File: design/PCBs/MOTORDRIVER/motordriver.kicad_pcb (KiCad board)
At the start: 2 copper layers, 1 part, among them U1 TMC4671-LA

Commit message: update docs
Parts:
- moved U1 26.6 mm to (145.0, 104.0)
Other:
- board outline added: 47.5 x 25 mm
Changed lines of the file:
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@@
 		(pad_to_mask_clearance 0)
 		(allow_soldermask_bridges_in_footprints no)
-		(grid_origin 165.027501 121.5)
+		(grid_origin 145.027501 104)
 		(pcbplotparams
 			(layerselection 0x00010fc_ffffffff)
@@
 	(footprint "Custom_Motor_Driver:QFN76_10P5X6P5_TRI"
 		(layer "F.Cu")
-		(at 165.027501 121.5)
+		(at 145.027501 104)
 		(tags "TMC4671-LA ")
 		(property "Reference" "U1"
@@
 		)
 	)
-	(gr_arc
-		(start 190.027501 135)
-		(mid 188.855928 137.828427)
-		(end 186.027501 139)
+	(gr_line
+		(start 167.627501 92.821401)
+		(end 167.627501 113.821401)
 		(stroke
-			(width 0.2)
+			(width 0.05)
 			(type default)
 		)
-		(layer "F.Cu")
+		(layer "Edge.Cuts")
 	)
-	(gr_arc
-		(start 144.027501 139)
-		(mid 141.199074 137.828427)
-		(end 140.027501 135)
+	(gr_line
+		(start 165.627501 115.821401)
+		(end 122.127501 115.821401)
 		(stroke
-			(width 0.2)
+			(width 0.05)
 			(type default)
 		)
-		(layer "F.Cu")
+		(layer "Edge.Cuts")
 	)
 	(gr_line
-		(start 140.027501 135)
-		(end 140.027501 105.5)
+		(start 120.127501 113.821401)
+		(end 120.127501 92.821401)
 		(stroke
-			(width 0.2)
+			(width 0.05)
 			(type default)
 		)
-		(layer "F.Cu")
+		(layer "Edge.Cuts")
 	)
 	(gr_arc
-		(start 186.027501 101.5)
-		(mid 188.855927 102.671573)
-		(end 190.027501 105.5)
+		(start 165.627501 90.821401)
+		(mid 167.041714 91.407188)
+		(end 167.627501 92.821401)
 		(stroke
-			(width 0.2)
+			(width 0.05)
 			(type default)
 		)
-		(layer "F.Cu")
+		(layer "Edge.Cuts")
 	)
-	(gr_line
-		(start 190.027501 105.5)
-		(end 190.027501 135)
+	(gr_arc
+		(start 120.127501 92.821401)
+		(mid 120.713287 91.407188)
+		(end 122.127501 90.821401)
 		(stroke
-			(width 0.2)
+			(width 0.05)
 			(type default)
 		)
-		(layer "F.Cu")
+		(layer "Edge.Cuts")
 	)
-	(gr_line
-		(start 186.027501 139)
-		(end 144.027501 139)
+	(gr_arc
+		(start 167.627501 113.821401)
+		(mid 167.041715 115.235615)
+		(end 165.627501 115.821401)
 		(stroke
-			(width 0.2)
+			(width 0.05)
 			(type default)
 		)
-		(layer "F.Cu")
+		(layer "Edge.Cuts")
 	)
 	(gr_line
-		(start 144.027501 101.5)
-		(end 186.027501 101.5)
+		(start 122.127501 90.821401)
+		(end 165.627501 90.821401)
 		(stroke
-			(width 0.2)
+			(width 0.05)
 			(type default)
 		)
-		(layer "F.Cu")
+		(layer "Edge.Cuts")
 	)
 	(gr_arc
-		(start 140.027501 105.5)
-		(mid 141.199074 102.671573)
-		(end 144.027501 101.5)
+		(start 122.127501 115.821401)
+		(mid 120.713287 115.235615)
+		(end 120.127501 113.821401)
 		(stroke
-			(width 0.2)
+			(width 0.05)
 			(type default)
 		)
-		(layer "F.Cu")
+		(layer "Edge.Cuts")
 	)
 )

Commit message: update motordriver
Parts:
- added U2: HIP2100_DFN, Package_DFN_QFN:DFN-12-1EP_4x4mm_P0.5mm_EP2.66x3.38mm, F.Cu at (130.6, 102.8)

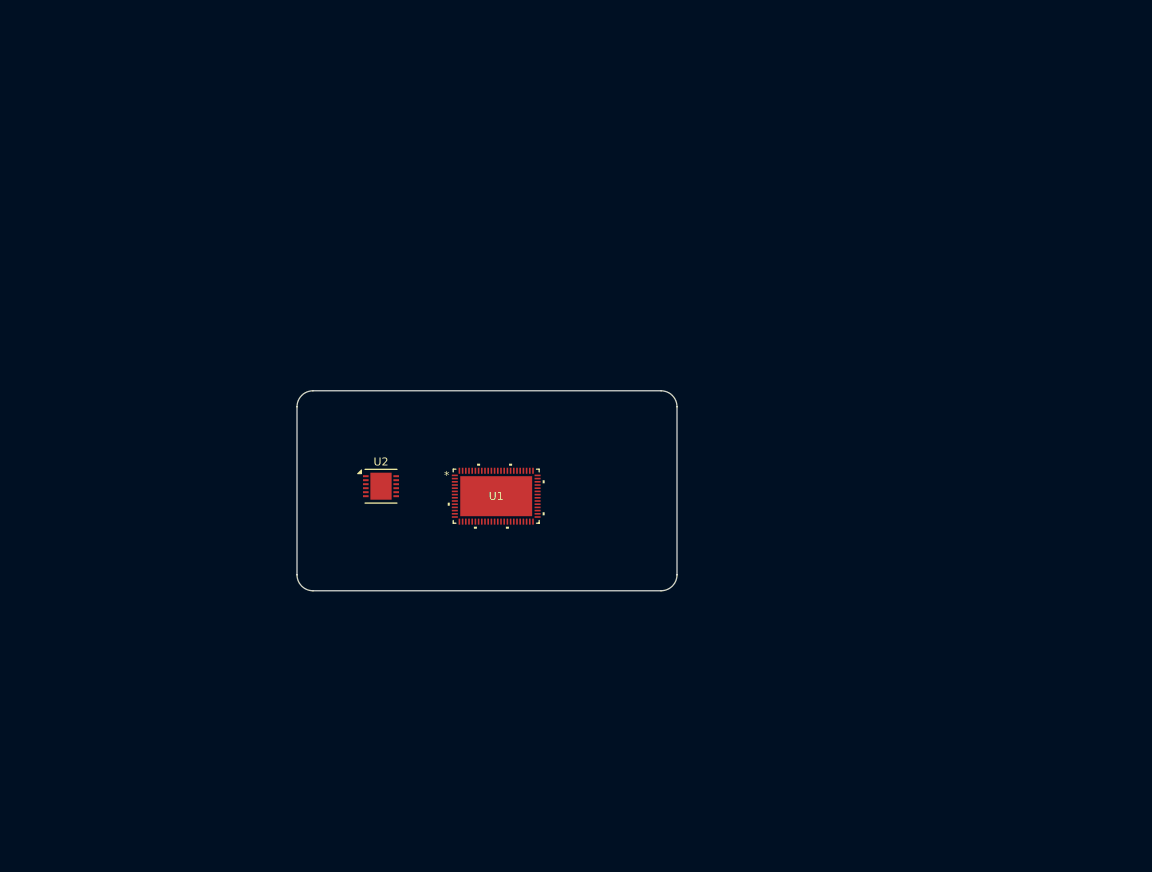
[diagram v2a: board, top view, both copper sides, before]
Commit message: cleaned up, added values and footprints
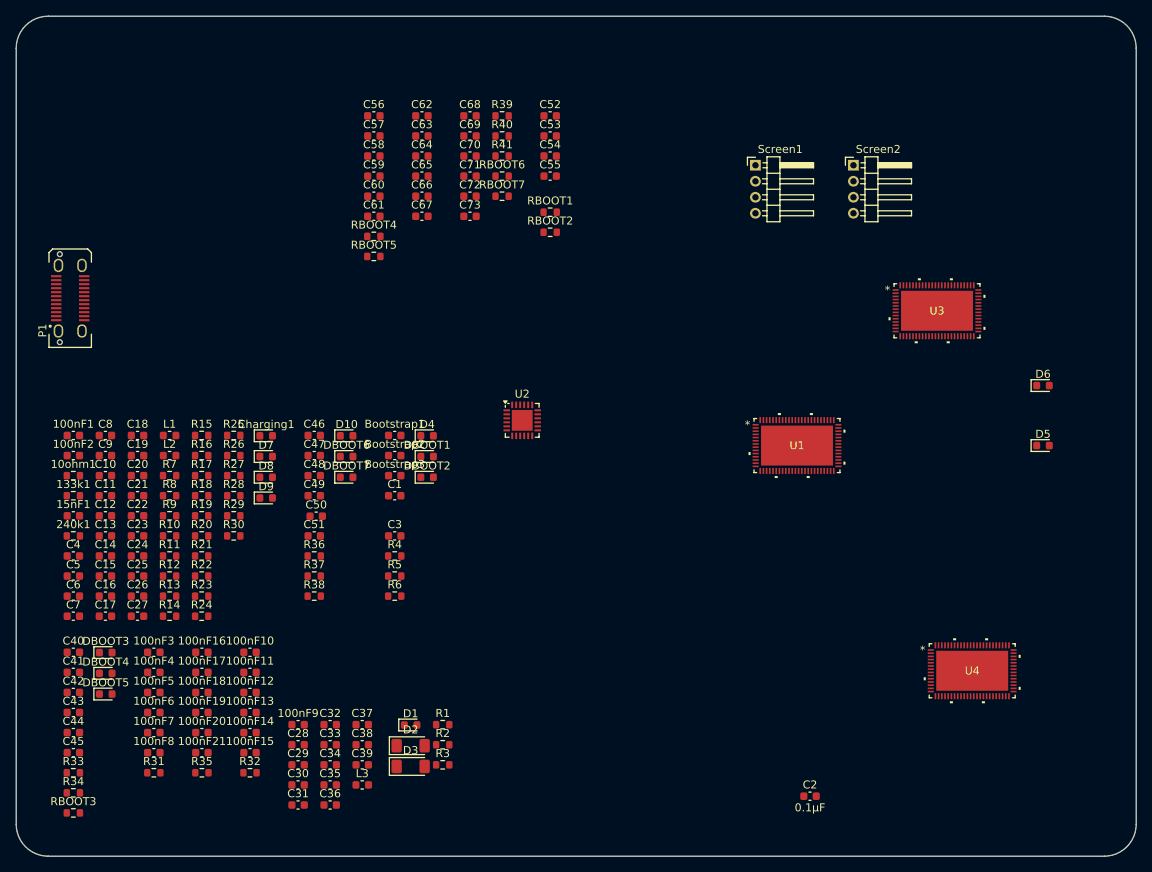
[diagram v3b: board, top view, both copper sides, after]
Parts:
- added 100nF1: C, Capacitor_SMD:C_0603_1608Metric, F.Cu at (92.2, 96.4)
- added 100nF10: C, Capacitor_SMD:C_0603_1608Metric, F.Cu at (114.3, 123.5)
- added 100nF11: C, Capacitor_SMD:C_0603_1608Metric, F.Cu at (114.3, 126.0)
- added 100nF12: C, Capacitor_SMD:C_0603_1608Metric, F.Cu at (114.3, 128.5)
- added 100nF13: C, Capacitor_SMD:C_0603_1608Metric, F.Cu at (114.3, 131.0)
- added 100nF14: C, Capacitor_SMD:C_0603_1608Metric, F.Cu at (114.3, 133.6)
- added 100nF15: C, Capacitor_SMD:C_0603_1608Metric, F.Cu at (114.3, 136.1)
- added 100nF16: C, Capacitor_SMD:C_0603_1608Metric, F.Cu at (108.2, 123.5)
- added 100nF17: C, Capacitor_SMD:C_0603_1608Metric, F.Cu at (108.2, 126.0)
- added 100nF18: C, Capacitor_SMD:C_0603_1608Metric, F.Cu at (108.2, 128.5)
- added 100nF19: C, Capacitor_SMD:C_0603_1608Metric, F.Cu at (108.2, 131.0)
- added 100nF2: C, Capacitor_SMD:C_0603_1608Metric, F.Cu at (92.2, 98.9)
- added 100nF20: C, Capacitor_SMD:C_0603_1608Metric, F.Cu at (108.2, 133.6)
- added 100nF21: C, Capacitor_SMD:C_0603_1608Metric, F.Cu at (108.2, 136.1)
- added 100nF3: C, Capacitor_SMD:C_0603_1608Metric, F.Cu at (102.2, 123.5)
- added 100nF4: C, Capacitor_SMD:C_0603_1608Metric, F.Cu at (102.2, 126.0)
- added 100nF5: C, Capacitor_SMD:C_0603_1608Metric, F.Cu at (102.2, 128.5)
- added 100nF6: C, Capacitor_SMD:C_0603_1608Metric, F.Cu at (102.2, 131.0)
- added 100nF7: C, Capacitor_SMD:C_0603_1608Metric, F.Cu at (102.2, 133.6)
- added 100nF8: C, Capacitor_SMD:C_0603_1608Metric, F.Cu at (102.2, 136.1)
- added 100nF9: C, Capacitor_SMD:C_0603_1608Metric, F.Cu at (120.3, 132.6)
- added 10ohm1: R, Resistor_SMD:R_0603_1608Metric, F.Cu at (92.2, 101.4)
- added 133k1: R, Resistor_SMD:R_0603_1608Metric, F.Cu at (92.2, 103.9)
- added 15nF1: C, Capacitor_SMD:C_0603_1608Metric, F.Cu at (92.2, 106.5)
- added 240k1: R, Resistor_SMD:R_0603_1608Metric, F.Cu at (92.2, 109.0)
- added Bootstrap1: 0.1µF, Capacitor_SMD:C_0603_1608Metric, F.Cu at (132.3, 96.4)
- added Bootstrap2: 0.1µF, Capacitor_SMD:C_0603_1608Metric, F.Cu at (132.3, 98.9)
- added Bootstrap3: 0.1µF, Capacitor_SMD:C_0603_1608Metric, F.Cu at (132.3, 101.4)
- added C1: 0.1µF, Capacitor_SMD:C_0603_1608Metric, F.Cu at (132.3, 103.9)
- added C10: 0.1µF, Capacitor_SMD:C_0603_1608Metric, F.Cu at (96.2, 101.4)
- added C11: 1µF, Capacitor_SMD:C_0603_1608Metric, F.Cu at (96.2, 103.9)
- added C12: 1µF, Capacitor_SMD:C_0603_1608Metric, F.Cu at (96.2, 106.5)
- added C13: 0.047µF, Capacitor_SMD:C_0603_1608Metric, F.Cu at (96.2, 109.0)
- added C14: 100nF, Capacitor_SMD:C_0603_1608Metric, F.Cu at (96.2, 111.5)
- added C15: 1µF, Capacitor_SMD:C_0603_1608Metric, F.Cu at (96.2, 114.0)
- added C16: 100nF, Capacitor_SMD:C_0603_1608Metric, F.Cu at (96.2, 116.5)
- added C17: 0.1µF, Capacitor_SMD:C_0603_1608Metric, F.Cu at (96.2, 119.0)
- added C18: 0.1µF, Capacitor_SMD:C_0603_1608Metric, F.Cu at (100.2, 96.4)
- added C19: 100nF, Capacitor_SMD:C_0603_1608Metric, F.Cu at (100.2, 98.9)
- added C2: 0.1µF, Capacitor_SMD:C_0603_1608Metric, F.Cu at (184.3, 141.5)
- added C20: 10µF, Capacitor_SMD:C_0603_1608Metric, F.Cu at (100.2, 101.4)
- added C21: 10µF, Capacitor_SMD:C_0603_1608Metric, F.Cu at (100.2, 103.9)
- added C22: 10nF, Capacitor_SMD:C_0603_1608Metric, F.Cu at (100.2, 106.5)
- added C23: 10µF, Capacitor_SMD:C_0603_1608Metric, F.Cu at (100.2, 109.0)
- added C24: 33nF, Capacitor_SMD:C_0603_1608Metric, F.Cu at (100.2, 111.5)
- added C25: 470pF, Capacitor_SMD:C_0603_1608Metric, F.Cu at (100.2, 114.0)
- added C26: 15nF, Capacitor_SMD:C_0603_1608Metric, F.Cu at (100.2, 116.5)
- added C27: 220pF, Capacitor_SMD:C_0603_1608Metric, F.Cu at (100.2, 119.0)
- added C28: 270µF, Capacitor_SMD:C_0603_1608Metric, F.Cu at (120.3, 135.1)
- added C29: 100nF, Capacitor_SMD:C_0603_1608Metric, F.Cu at (120.3, 137.6)
- added C3: 0.1µF, Capacitor_SMD:C_0603_1608Metric, F.Cu at (132.3, 109.0)
- added C30: 100nF, Capacitor_SMD:C_0603_1608Metric, F.Cu at (120.3, 140.1)
- added C31: 100nF, Capacitor_SMD:C_0603_1608Metric, F.Cu at (120.3, 142.6)
- added C32: 100nF, Capacitor_SMD:C_0603_1608Metric, F.Cu at (124.3, 132.6)
- added C33: 100nF, Capacitor_SMD:C_0603_1608Metric, F.Cu at (124.3, 135.1)
- added C34: 100nF, Capacitor_SMD:C_0603_1608Metric, F.Cu at (124.3, 137.6)
- added C35: 100nF, Capacitor_SMD:C_0603_1608Metric, F.Cu at (124.3, 140.1)
- added C36: 100nF, Capacitor_SMD:C_0603_1608Metric, F.Cu at (124.3, 142.6)
- added C37: 100nF, Capacitor_SMD:C_0603_1608Metric, F.Cu at (128.3, 132.6)
- added C38: 10µF, Capacitor_SMD:C_0603_1608Metric, F.Cu at (128.3, 135.1)
- added C39: 100nF, Capacitor_SMD:C_0603_1608Metric, F.Cu at (128.3, 137.6)
- added C4: 2.2µF, Capacitor_SMD:C_0603_1608Metric, F.Cu at (92.2, 111.5)
- added C40: 10µF, Capacitor_SMD:C_0603_1608Metric, F.Cu at (92.2, 123.5)
- added C41: 100nF, Capacitor_SMD:C_0603_1608Metric, F.Cu at (92.2, 126.0)
- added C42: 10µF, Capacitor_SMD:C_0603_1608Metric, F.Cu at (92.2, 128.5)
- added C43: 100nF, Capacitor_SMD:C_0603_1608Metric, F.Cu at (92.2, 131.0)
- added C44: 10µF, Capacitor_SMD:C_0603_1608Metric, F.Cu at (92.2, 133.6)
- added C45: 100nF, Capacitor_SMD:C_0603_1608Metric, F.Cu at (92.2, 136.1)
- added C46: 10µF, Capacitor_SMD:C_0603_1608Metric, F.Cu at (122.3, 96.4)
- added C47: 100nF, Capacitor_SMD:C_0603_1608Metric, F.Cu at (122.3, 98.9)
- added C48: 4.7µF, Capacitor_SMD:C_0603_1608Metric, F.Cu at (122.3, 101.4)
- added C49: 100nF, Capacitor_SMD:C_0603_1608Metric, F.Cu at (122.3, 103.9)
- added C5: ?F, Capacitor_SMD:C_0603_1608Metric, F.Cu at (92.2, 114.0)
- added C50: 100nF, Capacitor_SMD:C_0603_1608Metric, F.Cu at (122.5, 106.5)
- added C51: 100nF, Capacitor_SMD:C_0603_1608Metric, F.Cu at (122.3, 109.0)
- added C52: 100nF, Capacitor_SMD:C_0603_1608Metric, F.Cu at (151.8, 56.5)
- added C53: 100nF, Capacitor_SMD:C_0603_1608Metric, F.Cu at (151.8, 59.0)
- added C54: 100nF, Capacitor_SMD:C_0603_1608Metric, F.Cu at (151.8, 61.5)
- added C55: 100nF, Capacitor_SMD:C_0603_1608Metric, F.Cu at (151.8, 64.0)
- added C56: 0.1µF, Capacitor_SMD:C_0603_1608Metric, F.Cu at (129.7, 56.5)
- added C57: 0.1µF, Capacitor_SMD:C_0603_1608Metric, F.Cu at (129.7, 59.0)
- added C58: 0.1µF, Capacitor_SMD:C_0603_1608Metric, F.Cu at (129.7, 61.5)
- added C59: 0.1µF, Capacitor_SMD:C_0603_1608Metric, F.Cu at (129.7, 64.0)
- added C6: 10µF, Capacitor_SMD:C_0603_1608Metric, F.Cu at (92.2, 116.5)
- added C60: 0.1µF, Capacitor_SMD:C_0603_1608Metric, F.Cu at (129.7, 66.5)
- added C61: 0.1µF, Capacitor_SMD:C_0603_1608Metric, F.Cu at (129.7, 69.0)
- added C62: 100nF, Capacitor_SMD:C_0603_1608Metric, F.Cu at (135.7, 56.5)
- added C63: 100nF, Capacitor_SMD:C_0603_1608Metric, F.Cu at (135.7, 59.0)
- added C64: 100nF, Capacitor_SMD:C_0603_1608Metric, F.Cu at (135.7, 61.5)
- added C65: 100nF, Capacitor_SMD:C_0603_1608Metric, F.Cu at (135.7, 64.0)
- added C66: 100nF, Capacitor_SMD:C_0603_1608Metric, F.Cu at (135.7, 66.5)
- added C67: 100nF, Capacitor_SMD:C_0603_1608Metric, F.Cu at (135.7, 69.0)
- added C68: 0.1µF, Capacitor_SMD:C_0603_1608Metric, F.Cu at (141.8, 56.5)
- added C69: 0.1µF, Capacitor_SMD:C_0603_1608Metric, F.Cu at (141.8, 59.0)
- added C7: 100nF, Capacitor_SMD:C_0603_1608Metric, F.Cu at (92.2, 119.0)
- added C70: 0.1µF, Capacitor_SMD:C_0603_1608Metric, F.Cu at (141.8, 61.5)
- added C71: 0.1µF, Capacitor_SMD:C_0603_1608Metric, F.Cu at (141.8, 64.0)
- added C72: 0.1µF, Capacitor_SMD:C_0603_1608Metric, F.Cu at (141.8, 66.5)
- added C73: 0.1µF, Capacitor_SMD:C_0603_1608Metric, F.Cu at (141.8, 69.0)
- added C8: 100nF, Capacitor_SMD:C_0603_1608Metric, F.Cu at (96.2, 96.4)
- added C9: 0.1µF, Capacitor_SMD:C_0603_1608Metric, F.Cu at (96.2, 98.9)
- added Charging1: LED, Diode_SMD:D_0603_1608Metric, F.Cu at (116.3, 96.5)
- added D1: D, Diode_SMD:D_0603_1608Metric, F.Cu at (134.3, 132.6)
- added D10: D, Diode_SMD:D_0603_1608Metric, F.Cu at (126.3, 96.5)
- added D2: BZV55B2V4, Diode_SMD:D_MiniMELF, F.Cu at (134.3, 135.2)
- added D3: BZV55B2V4, Diode_SMD:D_MiniMELF, F.Cu at (134.3, 137.8)
- added D4: 470mV 500mA, Diode_SMD:D_0603_1608Metric, F.Cu at (136.4, 96.5)
- added D5: LED, Diode_SMD:D_0603_1608Metric, F.Cu at (213.4, 97.7)
- added D6: 385mV 500mA, Diode_SMD:D_0603_1608Metric, F.Cu at (213.4, 90.2)
- added D7: 470mV 500mA, Diode_SMD:D_0603_1608Metric, F.Cu at (116.3, 99.0)
- added D8: LED, Diode_SMD:D_0603_1608Metric, F.Cu at (116.3, 101.6)
- added D9: LED, Diode_SMD:D_0603_1608Metric, F.Cu at (116.3, 104.2)
- added DBOOT1: D, Diode_SMD:D_0603_1608Metric, F.Cu at (136.4, 99.0)
- added DBOOT2: D, Diode_SMD:D_0603_1608Metric, F.Cu at (136.4, 101.6)
- added DBOOT3: D, Diode_SMD:D_0603_1608Metric, F.Cu at (96.2, 123.5)
- added DBOOT4: D, Diode_SMD:D_0603_1608Metric, F.Cu at (96.2, 126.1)
- added DBOOT5: D, Diode_SMD:D_0603_1608Metric, F.Cu at (96.2, 128.7)
- added DBOOT6: D, Diode_SMD:D_0603_1608Metric, F.Cu at (126.3, 99.0)
- added DBOOT7: D, Diode_SMD:D_0603_1608Metric, F.Cu at (126.3, 101.6)
- added L1: ?H, Inductor_SMD:L_0603_1608Metric, F.Cu at (104.2, 96.4)
- added L2: 1µH 420µΩ, Inductor_SMD:L_0603_1608Metric, F.Cu at (104.2, 98.9)
- added L3: ?H, Inductor_SMD:L_0603_1608Metric, F.Cu at (128.3, 140.1)
- added P1: USB_C_Plug_USB2.0, Connector_USB:USB_C_Receptacle_JAE_DX07S024WJ3R400, F.Cu at (91.8, 79.2)
- added R1: 2.2Ω, Resistor_SMD:R_0603_1608Metric, F.Cu at (138.3, 132.6)
- added R10: 5.23kΩ, Resistor_SMD:R_0603_1608Metric, F.Cu at (104.2, 109.0)
- added R11: 30.1kΩ, Resistor_SMD:R_0603_1608Metric, F.Cu at (104.2, 111.5)
- added R12: 4.02kΩ, Resistor_SMD:R_0603_1608Metric, F.Cu at (104.2, 114.0)
- added R13: 20mΩ, Resistor_SMD:R_0603_1608Metric, F.Cu at (104.2, 116.5)
- added R14: 232kΩ, Resistor_SMD:R_0603_1608Metric, F.Cu at (104.2, 119.0)
- added R15: 32.4kΩ, Resistor_SMD:R_0603_1608Metric, F.Cu at (108.2, 96.4)
- added R16: 100kΩ, Resistor_SMD:R_0603_1608Metric, F.Cu at (108.2, 98.9)
- added R17: 32.4kΩ, Resistor_SMD:R_0603_1608Metric, F.Cu at (108.2, 101.4)
- added R18: 1kΩ, Resistor_SMD:R_0603_1608Metric, F.Cu at (108.2, 103.9)
- added R19: 10MΩ, Resistor_SMD:R_0603_1608Metric, F.Cu at (108.2, 106.5)
- added R2: 0.01Ω, Resistor_SMD:R_0603_1608Metric, F.Cu at (138.3, 135.1)
- added R20: 10Ω, Resistor_SMD:R_0603_1608Metric, F.Cu at (108.2, 109.0)
- added R21: 240kΩ, Resistor_SMD:R_0603_1608Metric, F.Cu at (108.2, 111.5)
- added R22: 133kΩ, Resistor_SMD:R_0603_1608Metric, F.Cu at (108.2, 114.0)
- added R23: 93.1kΩ, Resistor_SMD:R_0603_1608Metric, F.Cu at (108.2, 116.5)
- added R24: 23.2kΩ, Resistor_SMD:R_0603_1608Metric, F.Cu at (108.2, 119.0)
- added R25: 280kΩ, Resistor_SMD:R_0603_1608Metric, F.Cu at (112.2, 96.4)
- added R26: 2kΩ, Resistor_SMD:R_0603_1608Metric, F.Cu at (112.2, 98.9)
- added R27: 20kΩ, Resistor_SMD:R_0603_1608Metric, F.Cu at (112.2, 101.4)
- added R28: 9.09kΩ, Resistor_SMD:R_0603_1608Metric, F.Cu at (112.2, 103.9)
- added R29: 1kΩ, Resistor_SMD:R_0603_1608Metric, F.Cu at (112.2, 106.5)
- added R3: 0.01Ω, Resistor_SMD:R_0603_1608Metric, F.Cu at (138.3, 137.6)
- added R30: 10kΩ, Resistor_SMD:R_0603_1608Metric, F.Cu at (112.2, 109.0)
- added R31: 2mΩ, Resistor_SMD:R_0603_1608Metric, F.Cu at (102.2, 138.6)
- added R32: 10kΩ, Resistor_SMD:R_0603_1608Metric, F.Cu at (114.3, 138.6)
- added R33: 1kΩ, Resistor_SMD:R_0603_1608Metric, F.Cu at (92.2, 138.6)
- added R34: 1kΩ, Resistor_SMD:R_0603_1608Metric, F.Cu at (92.2, 141.1)
- added R35: 10kΩ, Resistor_SMD:R_0603_1608Metric, F.Cu at (108.2, 138.6)
- added R36: 0.01Ω, Resistor_SMD:R_0603_1608Metric, F.Cu at (122.3, 111.5)
- added R37: 0.01Ω, Resistor_SMD:R_0603_1608Metric, F.Cu at (122.3, 114.0)
- added R38: 10kΩ, Resistor_SMD:R_0603_1608Metric, F.Cu at (122.3, 116.5)
- added R39: 2.2Ω, Resistor_SMD:R_0603_1608Metric, F.Cu at (145.8, 56.5)
- added R4: 10Ω, Resistor_SMD:R_0603_1608Metric, F.Cu at (132.3, 111.5)
- added R40: 0.01Ω, Resistor_SMD:R_0603_1608Metric, F.Cu at (145.8, 59.0)
- added R41: 0.01Ω, Resistor_SMD:R_0603_1608Metric, F.Cu at (145.8, 61.5)
- added R5: 2Ω, Resistor_SMD:R_0603_1608Metric, F.Cu at (132.3, 114.0)
- added R6: 1MΩ, Resistor_SMD:R_0603_1608Metric, F.Cu at (132.3, 116.5)
- added R7: 100kΩ, Resistor_SMD:R_0603_1608Metric, F.Cu at (104.2, 101.4)
- added R8: 1.5kΩ, Resistor_SMD:R_0603_1608Metric, F.Cu at (104.2, 103.9)
- added R9: 4.02kΩ, Resistor_SMD:R_0603_1608Metric, F.Cu at (104.2, 106.5)
- added RBOOT1: 2.2Ω, Resistor_SMD:R_0603_1608Metric, F.Cu at (151.8, 68.5)
- added RBOOT2: 2.2Ω, Resistor_SMD:R_0603_1608Metric, F.Cu at (151.8, 71.0)
- added RBOOT3: 2.2Ω, Resistor_SMD:R_0603_1608Metric, F.Cu at (92.2, 143.6)
- added RBOOT4: 2.2Ω, Resistor_SMD:R_0603_1608Metric, F.Cu at (129.7, 71.5)
- added RBOOT5: 2.2Ω, Resistor_SMD:R_0603_1608Metric, F.Cu at (129.7, 74.0)
- added RBOOT6: 2.2Ω, Resistor_SMD:R_0603_1608Metric, F.Cu at (145.8, 64.0)
- added RBOOT7: 2.2Ω, Resistor_SMD:R_0603_1608Metric, F.Cu at (145.8, 66.5)
- added Screen1: Conn_01x04, Connector_PinHeader_2.00mm:PinHeader_1x04_P2.00mm_Horizontal, F.Cu at (177.4, 62.6)
- added Screen2: Conn_01x04, Connector_PinHeader_2.00mm:PinHeader_1x04_P2.00mm_Horizontal, F.Cu at (189.7, 62.6)
- added U3: TMC4671-LA, Custom_Motor_Driver:QFN76_10P5X6P5_TRI, F.Cu at (200.1, 80.8)
- added U4: TMC4671-LA, Custom_Motor_Driver:QFN76_10P5X6P5_TRI, F.Cu at (204.5, 125.8)
- U2: value HIP2100_DFN -> ATSAMD11D14A-M; footprint Package_DFN_QFN:DFN-12-1EP_4x4mm_P0.5mm_EP2.66x3.38mm -> Package_DFN_QFN:QFN-24-1EP_4x4mm_P0.5mm_EP2.6x2.6mm
- moved U1 38.1 mm to (182.6, 97.7)
- moved U2 19.5 mm to (148.3, 94.5)
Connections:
- U1 pad 1: unconnected-(U1-GPIO5/AENC_UX_MCD/DBGSPI_MOSI-Pad1) -> /driverIC/GPIO5
- U1 pad 12: unconnected-(U1-STATUS-Pad12) -> /driverIC/STATUS
- U1 pad 13: unconnected-(U1-VCCIO2-Pad13) -> +3.3V
- U1 pad 14: unconnected-(U1-GNDIO2-Pad14) -> GND
- U1 pad 16: unconnected-(U1-ADC_I0_POS-Pad16) -> /driverIC/ADC_I0_POS
- U1 pad 17: unconnected-(U1-ADC_I0_NEG-Pad17) -> +2V5
- U1 pad 18: unconnected-(U1-ADC_I1_POS-Pad18) -> /driverIC/ADC_I1_POS
- U1 pad 19: unconnected-(U1-ADC_I1_NEG-Pad19) -> +2V5
- U1 pad 2: unconnected-(U1-VCCIO1-Pad2) -> +3.3V
- U1 pad 23: unconnected-(U1-V5-Pad23) -> +5V
- U1 pad 24: unconnected-(U1-GNDA-Pad24) -> GND
- U1 pad 3: unconnected-(U1-GNDIO1-Pad3) -> GND
- U1 pad 36: unconnected-(U1-HALL_WY-Pad36) -> /driverIC/HALL_WY
- U1 pad 37: unconnected-(U1-HALL_B-Pad37) -> /driverIC/HALL_V
- U1 pad 38: unconnected-(U1-HALL_UX-Pad38) -> /driverIC/HALL_UX
- U1 pad 39: unconnected-(U1-PWM_UX1_H-Pad39) -> /driverIC/PWM_UX1_H
- U1 pad 4: unconnected-(U1-GPIO6/AENC_VN_MCD/DBGSPI_MISO-Pad4) -> /driverIC/GPIO6
- U1 pad 40: unconnected-(U1-PWM_UX1_L-Pad40) -> /driverIC/PWM_UX1_L
- U1 pad 41: unconnected-(U1-PWM_VX2_H-Pad41) -> /driverIC/PWM_VX2_H
- U1 pad 42: unconnected-(U1-PWM_VX2_L-Pad42) -> /driverIC/PWM_VX2_L
- U1 pad 43: unconnected-(U1-VCCIO3-Pad43) -> +3.3V
- U1 pad 44: unconnected-(U1-GNDIO3-Pad44) -> GND
- U1 pad 46: unconnected-(U1-PWM_WY1_H-Pad46) -> /driverIC/PWM_W1_H
- U1 pad 47: unconnected-(U1-PWM_WY1_L-Pad47) -> /driverIC/PWM_W1_L
- U1 pad 5: unconnected-(U1-GPIO7/AENC_WY_MCD/DBGSPI_TRG-Pad5) -> /driverIC/GPIO7
- U1 pad 51: unconnected-(U1-CLK-Pad51) -> /driverIC/CLK
- U1 pad 52: unconnected-(U1-VCCIO4-Pad52) -> +3.3V
- U1 pad 53: unconnected-(U1-GNDIO4-Pad53) -> GND
- U1 pad 54: unconnected-(U1-TEST-Pad54) -> GND
- U1 pad 55: unconnected-(U1-ENI-Pad55) -> /driverIC/ENI
- U1 pad 6: unconnected-(U1-SPI_NSCS-Pad6) -> /driverIC/TMC_CS
- U1 pad 61: unconnected-(U1-VCCIO5-Pad61) -> +3.3V
- U1 pad 62: unconnected-(U1-GNDIO5-Pad62) -> GND
- U1 pad 7: unconnected-(U1-SPI_SCK-Pad7) -> SPI_SCK
- U1 pad 72: unconnected-(U1-VCCIO6-Pad72) -> +3.3V
- U1 pad 73: unconnected-(U1-GNDIO6-Pad73) -> GND
- U1 pad 75: unconnected-(U1-GPIO3/AGPI_A_MCD/DBGSPI_NSCS-Pad75) -> /driverIC/GPIO3
- U1 pad 76: unconnected-(U1-GPIO4/AGPI_B_MCD/DBGSPI_SCK-Pad76) -> /driverIC/GPIO4
- U1 pad 8: unconnected-(U1-SPI_MOSI-Pad8) -> SPI_MOSI
- U1 pad 9: unconnected-(U1-SPI_MISO-Pad9) -> SPI_MISO
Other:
- board size 47.5 x 25 mm -> 140 x 105 mm

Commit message: new footprint and symbol system. added more footprints
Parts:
- removed Screen2: Conn_01x04, Connector_PinHeader_2.00mm:PinHeader_1x04_P2.00mm_Horizontal
- added C14: 100nF, Capacitor_SMD:C_0603_1608Metric, F.Cu at (215.3, 55.0)
- added C16: 10uF, Capacitor_SMD:C_0603_1608Metric, F.Cu at (215.3, 57.5)
- added C19: 100nF, Capacitor_SMD:C_0603_1608Metric, F.Cu at (215.3, 60.0)
- added C23: 10uF, Capacitor_SMD:C_0603_1608Metric, F.Cu at (215.3, 62.5)
- added C7: 100nF, Capacitor_SMD:C_0603_1608Metric, F.Cu at (215.3, 50.0)
- added C8: 10uF, Capacitor_SMD:C_0603_1608Metric, F.Cu at (215.3, 52.5)
- added DB1: Conn_01x02_Pin, Connector_PinHeader_2.54mm:PinHeader_1x02_P2.54mm_Vertical, F.Cu at (157.0, 116.8)
- added IC1: LM5109BSDX_NOPB, kuben_footprints:SON80P400X400X80-9N, F.Cu at (171.1, 103.5)
- added IC10: ATSAME53J18A-MF, kuben_footprints:QFN50P900X900X100-65N-D, F.Cu at (141.1, 85.8)
- added IC11: LM5109BSDX_NOPB, kuben_footprints:SON80P400X400X80-9N, F.Cu at (185.3, 103.5)
- added IC12: LM5109BSDX_NOPB, kuben_footprints:SON80P400X400X80-9N, F.Cu at (185.3, 109.1)
- added IC13: LM5109BSDX_NOPB, kuben_footprints:SON80P400X400X80-9N, F.Cu at (185.3, 114.8)
- added IC14: INA2181A2IDGSR, kuben_footprints:SOP50P490X110-10N, F.Cu at (185.8, 119.9)
- added IC15: LM5109BSDX_NOPB, kuben_footprints:SON80P400X400X80-9N, F.Cu at (196.5, 74.2)
- added IC16: LM5109BSDX_NOPB, kuben_footprints:SON80P400X400X80-9N, F.Cu at (196.5, 79.8)
- added IC17: LM5109BSDX_NOPB, kuben_footprints:SON80P400X400X80-9N, F.Cu at (196.5, 85.5)
- added IC18: INA2181A2IDGSR, kuben_footprints:SOP50P490X110-10N, F.Cu at (197.1, 90.6)
- added IC2: LM5109BSDX_NOPB, kuben_footprints:SON80P400X400X80-9N, F.Cu at (171.1, 109.1)
- added IC3: LM5109BSDX_NOPB, kuben_footprints:SON80P400X400X80-9N, F.Cu at (171.1, 114.8)
- added IC4: INA2181A2IDGSR, kuben_footprints:SOP50P490X110-10N, F.Cu at (171.6, 119.9)
- added IC7: BQ24133RGYR, kuben_footprints:BQ24133RGYR, F.Cu at (173.3, 88.8)
- added IC9: LM5176PWPR, kuben_footprints:SOP65P640X120-29N, F.Cu at (182.0, 77.0)
- added J1: IMU1, kuben_footprints:59453052110ECHLF, F.Cu at (140.8, 109.8)
- added J2: IMU2, kuben_footprints:59453052110ECHLF, F.Cu at (140.8, 116.7)
- added J3: Screw_Terminal_01x02, kuben_footprints:VN02A1500000G, F.Cu at (149.1, 119.3)
- added J4: 1-84952-1, kuben_footprints:1849521, F.Cu at (216.1, 104.5)
- added J5: 1-84952-1, kuben_footprints:1849521, F.Cu at (214.8, 81.5)
- added J6: 1-84952-1, kuben_footprints:1849521, F.Cu at (216.0, 128.0)
- added Q1: DMN3042L-7, kuben_footprints:SOT96P240X115-3N, F.Cu at (165.5, 102.9)
- added Q10: DMN3042L-7, kuben_footprints:SOT96P240X115-3N, F.Cu at (165.5, 82.7)
- added Q11: DMN3042L-7, kuben_footprints:SOT96P240X115-3N, F.Cu at (165.5, 87.2)
- added Q12: DMN3042L-7, kuben_footprints:SOT96P240X115-3N, F.Cu at (165.5, 91.8)
- added Q13: DMN3042L-7, kuben_footprints:SOT96P240X115-3N, F.Cu at (165.5, 96.3)
- added Q14: DMN3042L-7, kuben_footprints:SOT96P240X115-3N, F.Cu at (179.7, 102.9)
- added Q15: DMN3042L-7, kuben_footprints:SOT96P240X115-3N, F.Cu at (179.7, 107.5)
- added Q16: DMN3042L-7, kuben_footprints:SOT96P240X115-3N, F.Cu at (179.7, 112.0)
- added Q17: DMN3042L-7, kuben_footprints:SOT96P240X115-3N, F.Cu at (179.7, 116.5)
- added Q18: DMN3042L-7, kuben_footprints:SOT96P240X115-3N, F.Cu at (179.7, 121.1)
- added Q19: DMN3042L-7, kuben_footprints:SOT96P240X115-3N, F.Cu at (179.7, 125.7)
- added Q2: DMN3042L-7, kuben_footprints:SOT96P240X115-3N, F.Cu at (165.5, 107.5)
- added Q20: DMN3042L-7, kuben_footprints:SOT96P240X115-3N, F.Cu at (190.9, 73.6)
- added Q21: DMN3042L-7, kuben_footprints:SOT96P240X115-3N, F.Cu at (190.9, 78.2)
- added Q22: DMN3042L-7, kuben_footprints:SOT96P240X115-3N, F.Cu at (190.9, 82.7)
- added Q23: DMN3042L-7, kuben_footprints:SOT96P240X115-3N, F.Cu at (190.9, 87.2)
- added Q24: DMN3042L-7, kuben_footprints:SOT96P240X115-3N, F.Cu at (190.9, 91.8)
- added Q25: DMN3042L-7, kuben_footprints:SOT96P240X115-3N, F.Cu at (190.9, 96.3)
- added Q3: DMN3042L-7, kuben_footprints:SOT96P240X115-3N, F.Cu at (165.5, 112.0)
- added Q4: DMN3042L-7, kuben_footprints:SOT96P240X115-3N, F.Cu at (165.5, 116.5)
- added Q5: DMN3042L-7, kuben_footprints:SOT96P240X115-3N, F.Cu at (165.5, 121.1)
- added Q6: DMN3042L-7, kuben_footprints:SOT96P240X115-3N, F.Cu at (165.5, 125.7)
- added Q7: DMN3042L-7, kuben_footprints:SOT96P240X115-3N, F.Cu at (165.5, 73.6)
- added Q8: DMN3042L-7, kuben_footprints:SOT96P240X115-3N, F.Cu at (165.5, 78.2)
- added Q9: DMPH6050SK3-13, kuben_footprints:DMPH6050SK313, F.Cu at (172.7, 78.3)
- added S1: ~, Connector_PinHeader_2.54mm:PinHeader_1x03_P2.54mm_Vertical, F.Cu at (148.4, 107.2)
- added S2: ~, Connector_PinHeader_2.54mm:PinHeader_1x03_P2.54mm_Vertical, F.Cu at (153.1, 107.2)
- added S3: ~, Connector_PinHeader_2.54mm:PinHeader_1x03_P2.54mm_Vertical, F.Cu at (157.7, 107.2)
- added U5: LD1117S25TR_SOT223, Package_TO_SOT_SMD:SOT-223-3_TabPin2, F.Cu at (208.3, 52.9)
- added U6: LD1117S50TR_SOT223, Package_TO_SOT_SMD:SOT-223-3_TabPin2, F.Cu at (208.3, 61.2)
- added U7: LD1117S33TR_SOT223, Package_TO_SOT_SMD:SOT-223-3_TabPin2, F.Cu at (208.3, 69.5)
- U1, U3, U4: footprint Custom_Motor_Driver:QFN76_10P5X6P5_TRI -> kuben_footprints:QFN76_10P5X6P5_TRI-L
- moved U1 38.2 mm to (206.5, 127.5), turned to 90 degrees
- moved D6 29.4 mm to (191.5, 70.5)
- moved U2 20.5 mm to (167.9, 88.3)
- moved U4 20.4 mm to (206.5, 105.5), turned to -90 degrees
- moved Screen1 13.8 mm to (174.5, 49.1), turned to 90 degrees
- moved D5 10.1 mm to (205.8, 91.0)
- moved U3 6.40 mm to (206.5, 81.0), turned to -90 degrees
- moved 100nF19 2.25 mm to (106.5, 132.5)
- moved 100nF6 2.25 mm to (100.5, 132.5)
- moved C28 2.25 mm to (118.5, 136.5)
- moved C31 2.25 mm to (118.5, 144.0)
- moved C33 2.25 mm to (122.5, 136.5)
- moved C36 2.25 mm to (122.5, 144.0)
- moved D1 2.25 mm to (132.6, 134.0)
- moved D2 2.25 mm to (132.6, 136.6)
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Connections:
- net /input/D+ renamed /IO/D+
- net /input/D- renamed /IO/D-
- D2 pad 2: /input/BAT_12V -> /IO/BAT_12V
- Screen1 pad 1: /input/OLED_SCL -> /IO/OLED_SCL
- Screen1 pad 2: /input/OLED_SDA -> /IO/OLED_SDA
- U1 pad 10: unconnected-(U1-UART_RXD-Pad10) -> /driverIC/tmc_rx
- U1 pad 11: unconnected-(U1-UART_TXD-Pad11) -> /driverIC/tmc_tx
- U3 pad 10: unconnected-(U3-UART_RXD-Pad10) -> /driverIC1/tmc_rx
- U3 pad 11: unconnected-(U3-UART_TXD-Pad11) -> /driverIC1/tmc_tx
- U4 pad 10: unconnected-(U4-UART_RXD-Pad10) -> /driverIC2/tmc_rx
- U4 pad 11: unconnected-(U4-UART_TXD-Pad11) -> /driverIC2/tmc_tx
